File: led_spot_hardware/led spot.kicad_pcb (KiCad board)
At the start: 4 copper layers, 50 x 50 mm, 49 parts, among them K1 PWR, P1 mod_jack_in, P2 LED, P3 SWD, Q1 FDN5618P, U1 LM2594-HV, U2 STM32F030-20, U3 2CH-TVS, U4 ISL83485IBZ, U5 TPS92511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

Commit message: improvements to LED spot
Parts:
- moved P1 4.00 mm to (175.0, 203.0)
- moved HOLE 3.00 mm to (156.0, 199.0)
- moved HOLE 3.00 mm to (194.0, 199.0)
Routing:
- net N-0000028: track 16.4 -> 21.0 mm
- net N-0000025: track 19.9 -> 23.4 mm
- net GND: track 68.0 -> 64.7 mm, vias 26 -> 24
- net N-000004: track 23.2 -> 24.0 mm
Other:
- board size 50 x 50 mm -> 50 x 49.9 mm

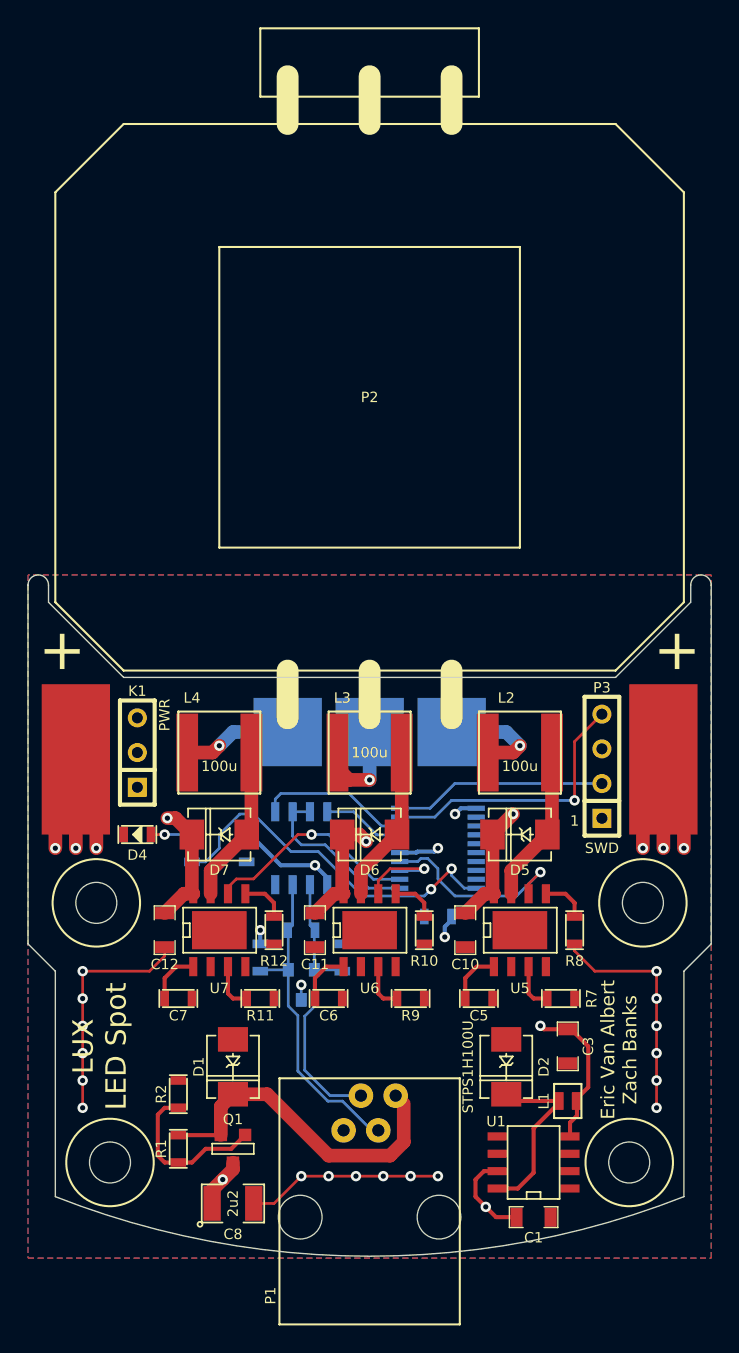
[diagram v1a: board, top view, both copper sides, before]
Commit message: finish updating LED spot
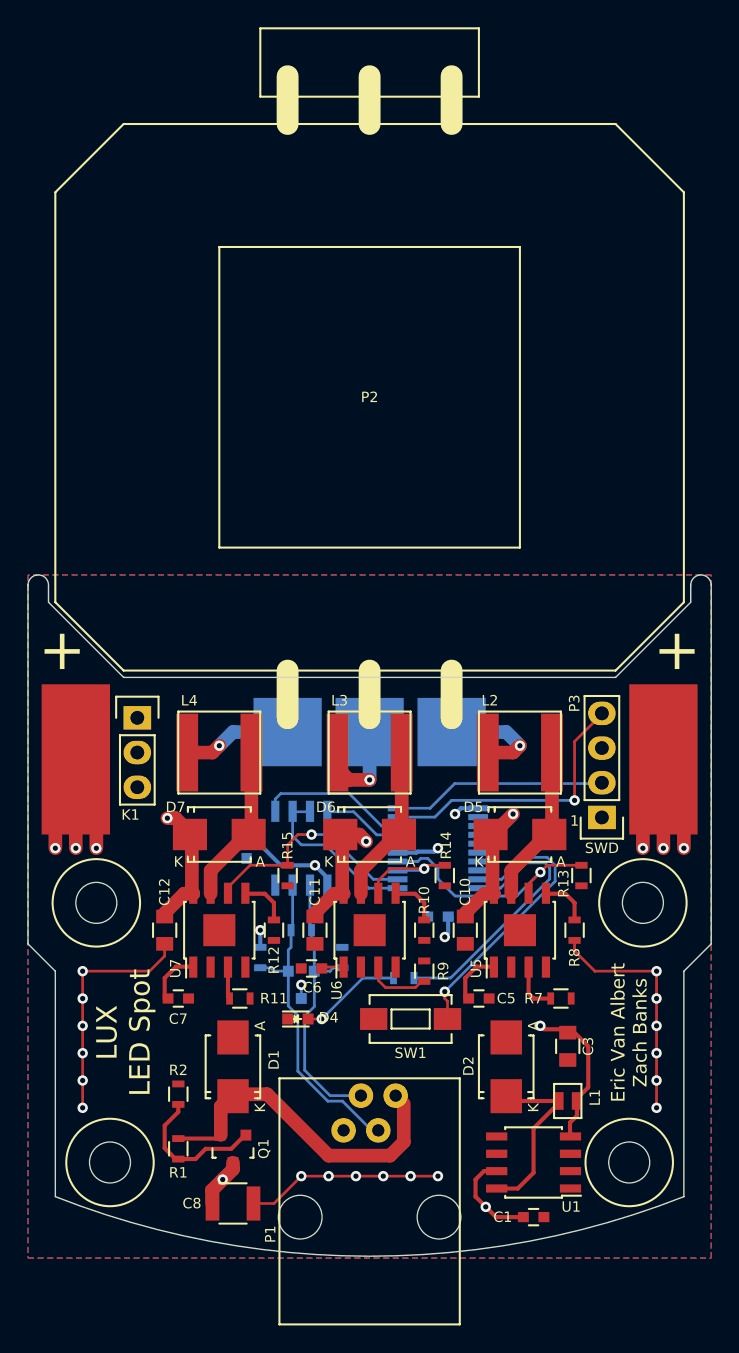
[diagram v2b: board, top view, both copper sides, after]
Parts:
- added R13: 1K, Resistors_SMD:R_0603, F.Cu at (190.5, 178.0)
- added R14: 1K, Resistors_SMD:R_0603, F.Cu at (180.5, 178.0)
- added R15: 1K, Resistors_SMD:R_0603, F.Cu at (169.0, 178.0)
- added SW1: SW_Push, Buttons_Switches_SMD:SW_SPST_EVQPE1, F.Cu at (178.0, 188.5)
- C1: footprint SA0805 -> Capacitors_SMD:C_0603
- C10, C11, C12, C3: footprint SA0805 -> Capacitors_SMD:C_0805
- C2, C5, C6, C7, C9: footprint SA0603 -> Capacitors_SMD:C_0603
- C8: footprint SM1210 -> Capacitors_SMD:C_1210
- D1, D2, D5, D6, D7: footprint DO-214AA(SMB) -> Diodes_SMD:SMB_Standard
- D4: footprint SA0603_LED -> LEDs:LED_0603
- K1: footprint SIL-3 -> Pin_Headers:Pin_Header_Straight_1x03
- L1: footprint VLF-M -> custom:VLF-M
- L2, L3, L4: footprint NRS6028T101MMGJ -> custom:NRS6028T101MMGJ
- P1: footprint Assman-6p4c -> custom:Assman-6p4c
- P3: footprint SIL-4 -> Pin_Headers:Pin_Header_Straight_1x04
- Q1: footprint SOT23GDS -> TO_SOT_Packages_SMD:SOT-23
- R1, R2, R3, R4, R5, R6: footprint SA0603 -> Resistors_SMD:R_0603
- R10, R12, R8: value 20K -> 22K; footprint SA0603 -> Resistors_SMD:R_0603
- R11, R7, R9: value 5K -> 3K3; footprint SA0603 -> Resistors_SMD:R_0603
- U1, U4: footprint SO8E -> Housings_SOIC:SOIC-8_3.9x4.9mm_Pitch1.27mm
- U2: footprint TSSOP20 -> Housings_SSOP:TSSOP-20_4.4x6.5mm_Pitch0.65mm
- U3: footprint SOT23 -> TO_SOT_Packages_SMD:SOT-23
- U5, U6, U7: footprint SO8_WITH_EP -> Housings_SOIC:SOIC-8-1EP_3.9x4.9mm_Pitch1.27mm
- moved R6 18.2 mm to (177.5, 185.5), turned to 180 degrees
- moved D4 17.9 mm to (169.7, 188.5), turned to 0 degrees
- moved P3 3.75 mm to (192.0, 173.8), turned to 180 degrees
- moved K1 2.54 mm to (158.0, 166.5), turned to 0 degrees
- moved C6 2.53 mm to (170.8, 184.8), turned to 180 degrees
- moved R9 2.24 mm to (179.0, 185.0), turned to 270 degrees
- moved R11 1.50 mm to (165.5, 187.0)
- turned D1 to 90 degrees
- turned D2 to 90 degrees
- turned D5 to 0 degrees
- turned D6 to 0 degrees
- turned D7 to 0 degrees
- turned Q1 to 180 degrees
- turned U1 to 180 degrees
- turned U2 to 180 degrees
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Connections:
- net /DriverB/DIM renamed /PWM_B
- net /DriverG/DIM renamed /PWM_G
- net /DriverR/DIM renamed /PWM_R
- D1 pad 1: GND -> Net-(D1-Pad1)
- D1 pad 2: N-000004 -> GND
- D2 pad 1: GND -> Net-(D2-Pad1)
- D2 pad 2: N-000006 -> GND
- D4 pad 1: N-0000019 -> GND
- D4 pad 2: GND -> Net-(D4-Pad2)
- D5 pad 1: N-0000032 -> +48V
- D5 pad 2: +48V -> Net-(D5-Pad2)
- D6 pad 1: N-0000035 -> +48V
- D6 pad 2: +48V -> Net-(D6-Pad2)
- D7 pad 1: N-0000039 -> +48V
- D7 pad 2: +48V -> Net-(D7-Pad2)
- L1 pad 1: N-000006 -> Net-(D2-Pad1)
- L2 pad 1: N-0000032 -> Net-(D5-Pad2)
- L2 pad 2: /DriverR/LEDCat -> /LED_R
- L3 pad 1: N-0000035 -> Net-(D6-Pad2)
- L3 pad 2: /DriverG/LEDCat -> /LED_G
- L4 pad 1: N-0000039 -> Net-(D7-Pad2)
- L4 pad 2: /DriverB/LEDCat -> /LED_B
- P1 pad 4: N-000004 -> Net-(D1-Pad1)
- R1 pad 1: N-000004 -> Net-(D1-Pad1)
- R1 pad 2: N-000002 -> Net-(Q1-Pad1)
- R2 pad 1: N-000002 -> Net-(Q1-Pad1)
- R6 pad 2: N-0000019 -> Net-(D4-Pad2)
- U1 pad 8: N-000006 -> Net-(D2-Pad1)
- U2 pad 9: N-000009 -> /USR_BUTTON
- U5 pad 7: N-0000032 -> Net-(D5-Pad2)
- U6 pad 7: N-0000035 -> Net-(D6-Pad2)
- U7 pad 7: N-0000039 -> Net-(D7-Pad2)
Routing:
- net Net-(D1-Pad1): track 0.00 -> 24.1 mm
- net N-000004: track 24.0 -> 0.00 mm
- net /USR_BUTTON: track 0.00 -> 21.2 mm, vias 0 -> 1
- net N-000006: track 13.2 -> 0.00 mm
- net Net-(D2-Pad1): track 0.00 -> 13.2 mm
- net N-000002: track 12.1 -> 0.00 mm
- net Net-(D6-Pad2): track 0.00 -> 11.6 mm
- net Net-(D5-Pad2): track 0.00 -> 11.6 mm
- net N-0000035: track 11.6 -> 0.00 mm
- net N-0000032: track 11.6 -> 0.00 mm
- net Net-(D7-Pad2): track 0.00 -> 11.6 mm
- net N-0000039: track 11.6 -> 0.00 mm
- net Net-(Q1-Pad1): track 0.00 -> 10.6 mm
- net Net-(D4-Pad2): track 0.00 -> 7.49 mm, vias 0 -> 1
- net /USR_LED: track 27.0 -> 19.9 mm, vias 2 -> 0
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
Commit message: rev 2 gerbers
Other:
- board text added: "rev 2"
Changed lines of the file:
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@@
   (general
     (links 125)
-    (no_connects 8)
-    (area 149.949999 115.724999 200.050001 221.475)
+    (no_connects 0)
+    (area 140.150002 115.724999 200.050001 211.125001)
     (thickness 1.6)
-    (drawings 20)
+    (drawings 23)
     (tracks 306)
     (zones 0)
@@
     (35 F.Paste user)
     (36 B.SilkS user)
-    (37 F.SilkS user hide)
+    (37 F.SilkS user)
     (38 B.Mask user)
     (39 F.Mask user)
@@
   )
   (setup
-    (last_trace_width 0.3)
+    (last_trace_width 0.2)
     (user_trace_width 0.3)
     (user_trace_width 1)
@@
     (visible_elements FFFFEF7F)
     (pcbplotparams
-      (layerselection 0x00030_80000001)
+      (layerselection 0x010f0_80000007)
       (usegerberextensions true)
       (excludeedgelayer true)
@@
     )
   )
+  (gr_text "rev 2" (at 159 190 90) (layer F.SilkS)
+    (effects (font (size 0.762 0.762) (thickness 0.13)))
+  )
+  (dimension 50 (width 0.3) (layer Dwgs.User)
+    (gr_text "50.000 mm" (at 175 152.65) (layer Dwgs.User)
+      (effects (font (size 1.5 1.5) (thickness 0.3)))
+    )
+    (feature1 (pts (xy 200 156) (xy 200 151.3)))
+    (feature2 (pts (xy 150 156) (xy 150 151.3)))
+    (crossbar (pts (xy 150 154) (xy 200 154)))
+    (arrow1a (pts (xy 200 154) (xy 198.873496 154.586421)))
+    (arrow1b (pts (xy 200 154) (xy 198.873496 153.413579)))
+    (arrow2a (pts (xy 150 154) (xy 151.126504 154.586421)))
+    (arrow2b (pts (xy 150 154) (xy 151.126504 153.413579)))
+  )
+  (dimension 50 (width 0.3) (layer Dwgs.User)
+    (gr_text "50.000 mm" (at 146.650001 181 270) (layer Dwgs.User)
+      (effects (font (size 1.5 1.5) (thickness 0.3)))
+    )
+    (feature1 (pts (xy 150 206) (xy 145.300001 206)))
+    (feature2 (pts (xy 150 156) (xy 145.300001 156)))
+    (crossbar (pts (xy 148.000001 156) (xy 148.000001 206)))
+    (arrow1a (pts (xy 148.000001 206) (xy 147.41358 204.873496)))
+    (arrow1b (pts (xy 148.000001 206) (xy 148.586422 204.873496)))
+    (arrow2a (pts (xy 148.000001 156) (xy 147.41358 157.126504)))
+    (arrow2b (pts (xy 148.000001 156) (xy 148.586422 157.126504)))
+  )
   (gr_line (start 152 185) (end 152 201.5) (layer Edge.Cuts) (width 0.1))
   (gr_line (start 198 185) (end 198 201.5) (layer Edge.Cuts) (width 0.1))
@@
     (effects (font (size 1 1) (thickness 0.2)))
   )
-  (gr_text "LUX\nLED Spot" (at 157 189.5 90) (layer F.SilkS)
+  (gr_text "LUX\nLED Spot" (at 156 189.5 90) (layer F.SilkS)
     (effects (font (size 1.5 1.5) (thickness 0.3)))
   )
